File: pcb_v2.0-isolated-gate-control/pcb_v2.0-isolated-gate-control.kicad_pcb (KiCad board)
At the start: 4 copper layers, 170 x 110 mm, 195 parts, among them J1 ServoLock, J10 Buttons, J11 2x encoder, J12 limit-g2, J13 Relay VFD2 [NO, COM, NC], J14 GND-P, J15 OD, J16 Power-LightBarrier-12V, J17 3V3 5V VDD, J18 GNDD, J19 OD, J2 supply, J20 OD, J21 limit-g1, J3 12V 5V, J4 light-barrier, switch, J5 GND-P, J6 2x remoteControl, J7 Relay VFD1 [NO, COM, NC], J8 RS485, J9 Conn_01x03_Pin, K1 RT314A24, K2 RT314A24, Q1 2N7000, Q2 2N7000, Q3 IRF5305, Q6 IRF5305, U1 ULN2003, U2 esp32-devkit-v1_30Pin, U3 74HC04, U4 MAX485E, U5 L78S05CV_TO220

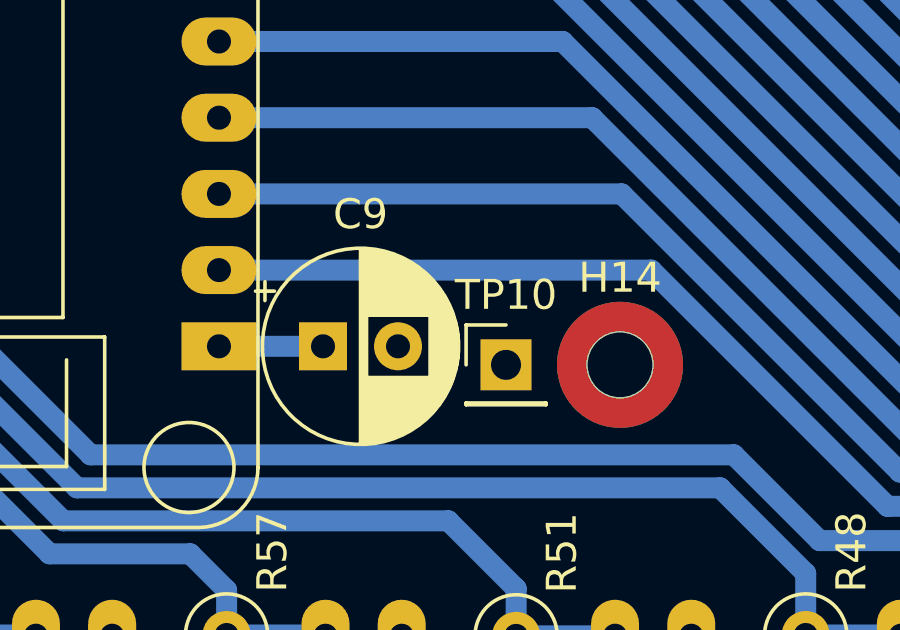
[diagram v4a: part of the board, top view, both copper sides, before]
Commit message: pcb: fix minor layout issues (missing text, spacing)
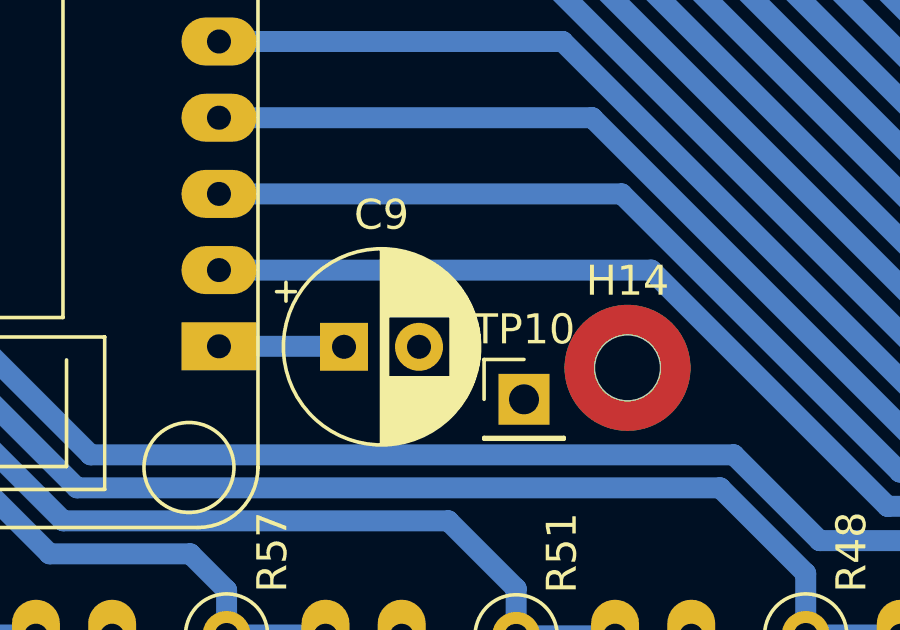
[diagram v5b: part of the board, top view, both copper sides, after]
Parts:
- moved TP10 1.30 mm to (75.7, 86.3)
- moved C9 0.70 mm to (69.7, 84.6)
- moved H14 0.27 mm to (79.2, 85.3)
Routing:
- net Net-(U2-EN): track 3.43 -> 4.14 mm
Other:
- board text added: "12V GND"
- board text added: "5V"
- board text added: "Changelog since Tag {dblquote}pcb-for-V2-milled{dblquote}: - fix swapped 12V/GND testpoint text - add missing testpoint text: 5V, isolated-GND, - reduce title text thickness from 0.4 to 0.35 - more space between EN-C and esp32"
- board text removed: "GND 12V"
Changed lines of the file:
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@@
 	(footprint "Connector_PinHeader_2.54mm:PinHeader_1x01_P2.54mm_Vertical"
 		(layer "F.Cu")
-		(at 75.1 85.2)
+		(at 75.7 86.35)
 		(descr "Through hole straight pin header, 1x01, 2.54mm pitch, single row")
 		(tags "Through hole pin header THT 1x01 2.54mm single row")
@@
 	(footprint "mountingHoles_libJonny:MountingHole_2.2mm_NPTH-with-pad_DRC-clearance-error"
 		(layer "F.Cu")
-		(at 78.9 85.2)
+		(at 79.15 85.3)
 		(descr "Mounting Hole 2.2mm, M2, ISO14580")
 		(tags "mounting hole 2.2mm m2 iso14580")
@@
 	(footprint "Capacitor_THT:CP_Radial_D6.3mm_P2.50mm"
 		(layer "F.Cu")
-		(at 69 84.582)
+		(at 69.7 84.6)
 		(descr "CP, Radial series, Radial, pin pitch=2.50mm, , diameter=6.3mm, Electrolytic Capacitor")
 		(tags "CP Radial series Radial pin pitch 2.50mm  diameter 6.3mm Electrolytic Capacitor")
@@
 		(layer "User.7")
 	)
+	(gr_text "Changelog since Tag {dblquote}pcb-for-V2-milled{dblquote}:\n - fix swapped 12V/GND testpoint text\n - add missing testpoint text: 5V, isolated-GND,\n - reduce title text thickness from 0.4 to 0.35\n - more space between EN-C and esp32"
+		(at 211.1 38.55 0)
+		(layer "User.2")
+		(effects
+			(font
+				(size 2 2)
+				(thickness 0.3)
+				(bold yes)
+			)
+			(justify left bottom)
+		)
+	)
 	(gr_text "Layer User7: Marked pads to solder on top side"
 		(at 37.592 145.288 0)
@@
 		)
 	)
+	(gr_text "5V"
+		(at 130.95 56.2 0)
+		(layer "User.9")
+		(effects
+			(font
+				(size 1.3 1.3)
+				(thickness 0.3)
+				(bold yes)
+			)
+			(justify bottom)
+		)
+	)
 	(gr_text "GND      GND"
 		(at 161.544 27.686 180)
@@
 			(font
 				(size 2.2 2.2)
-				(thickness 0.4)
-				(bold yes)
+				(thickness 0.35)
 			)
 			(justify left bottom)
@@
 		)
 	)
+	(gr_text "GND"
+		(at 75.75 89.6 0)
+		(layer "User.9")
+		(effects
+			(font
+				(size 1.3 1.3)
+				(thickness 0.3)
+				(bold yes)
+			)
+			(justify bottom)
+		)
+	)
 	(gr_text "Fuse-PCB"
 		(at 191.897 42.8498 90)
@@
 		)
 	)
-	(gr_text "GND 12V"
-		(at 147.7772 30.1244 0)
+	(gr_text "12V GND"
+		(at 147.85 29.95 0)
 		(layer "User.9")
 		(effects
@@
 	)
 	(segment
-		(start 69 84.582)
+		(start 69.7 84.6)
+		(end 69.682 84.582)
+		(width 0.7)
+		(layer "B.Cu")
+		(net 2)
+	)
+	(segment
+		(start 69.682 84.582)
 		(end 65.565903 84.582)
 		(width 0.7)
